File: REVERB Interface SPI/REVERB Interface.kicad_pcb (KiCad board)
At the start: 2 copper layers, 90.2 x 95.9 mm, 49 parts, among them J1 RPiZeroW, J2 Iridium, J3 APRS, J4 Antenna, J6 USB_B_Micro, J7 USB, J8 USBPOGO, M1 MountingHole_Pad, M2 MountingHole_Pad, M3 MountingHole_Pad, M4 MountingHole_Pad, M5 PiMount, M6 PiMount, M7 PiMount, M8 PiMount, U1 LSM9DS1BOB, U2 MAX3232, U3 CY7C65213-28PVXI

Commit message: spi edits
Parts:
- removed J6: USB_B_Micro, REVERB Interface:AdafruitMicroB
- removed J7: USB, Connector_PinSocket_2.54mm:PinSocket_1x02_P2.54mm_Vertical
- removed J8: USBPOGO, Connector_PinSocket_2.54mm:PinSocket_1x02_P2.54mm_Vertical
- added C9: 33pF, Capacitor_SMD:C_0805_2012Metric_Pad1.18x1.45mm_HandSolder, F.Cu at (230.2, 125.1)
- added R7: 1K, Resistor_SMD:R_0805_2012Metric_Pad1.20x1.40mm_HandSolder, F.Cu at (225.4, 128.1)
- added R8: 1K, Resistor_SMD:R_0805_2012Metric_Pad1.20x1.40mm_HandSolder, F.Cu at (230.1, 128.1)
- added Y1: 1.8432MHz, Crystal:Crystal_HC49-U_Vertical, F.Cu at (227.0, 120.3)
- C6: value 4.7uF -> 10uF
- C8: value 1uF -> 22pF
- JP3: value USBUARTRX -> SPIUARTRX
- JP4: value USBUARTTX -> SPIUARTTX
- U3: value CY7C65213-28PVXI -> SC16IS752IPW; footprint Package_SO:SSOP-28_5.3x10.2mm_P0.65mm -> Package_SO:TSSOP-28_4.4x9.7mm_P0.65mm
- moved C7 90.0 mm to (235.9, 134.6), turned to 0 degrees
- moved U3 83.9 mm to (240.3, 122.6)
- moved C6 82.1 mm to (231.1, 134.6), turned to 0 degrees
- moved C8 76.4 mm to (225.4, 125.1), turned to 0 degrees
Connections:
- C6 pad 1: /SW7 -> /SW10
- C7 pad 1: /SW7 -> /SW10
- D1 pad 1: /USBUARTTX -> /SPIUARTTX
- D2 pad 1: /USBUARTRX -> /SPIUARTRX
- H2 pad 16: /SW7 -> (no net)
- H2 pad 20: (no net) -> /SW10
- J1 pad 19: (no net) -> /SPIMOSI
- J1 pad 21: (no net) -> /SPIMISO
- J1 pad 23: (no net) -> /SPISCK
- J1 pad 24: (no net) -> /SPICE0
- JP3 pad 2: /USBUARTRX -> /SPIUARTRX
- JP4 pad 2: /USBUARTTX -> /SPIUARTTX
- R1 pad 1: /SW7 -> /SW10
- R2 pad 1: /SW7 -> /SW10
- R3 pad 1: /SW7 -> /SW10
- U3 pad 1: /USBUARTTX -> (no net)
- U3 pad 10: (no net) -> /SPICE0
- U3 pad 11: (no net) -> /SPIMOSI
- U3 pad 12: (no net) -> /SPIMISO
- U3 pad 13: (no net) -> /SPISCK
- U3 pad 14: (no net) -> GND
- U3 pad 15: /D+ -> Net-(R7-Pad2)
- U3 pad 16: /D- -> (no net)
- U3 pad 17: Net-(C8-Pad1) -> (no net)
- U3 pad 18: GND -> (no net)
- U3 pad 20: /SW7 -> (no net)
- U3 pad 21: GND -> (no net)
- U3 pad 22: (no net) -> GND
- U3 pad 3: (no net) -> /SPIUARTTX
- U3 pad 4: /SW7 -> /SPIUARTRX
- U3 pad 5: /USBUARTRX -> Net-(R8-Pad2)
- U3 pad 6: (no net) -> Net-(C8-Pad1)
- U3 pad 7: GND -> Net-(C9-Pad1)
- U3 pad 8: (no net) -> /SW10
- U3 pad 9: (no net) -> GND
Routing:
- net /SW7: track 122.6 -> 0.00 mm, vias 2 -> 0
- net /D+: track 79.8 -> 0.00 mm
- net /D-: track 73.7 -> 0.00 mm
- net /USBUARTRX: track 26.0 -> 0.00 mm, vias 2 -> 0
- net /USBUARTTX: track 23.8 -> 0.00 mm
- net GND: track 34.4 -> 19.7 mm, vias 18 -> 14
- net Net-(C8-Pad1): track 11.4 -> 0.00 mm, vias 2 -> 0
- net /SPIUARTTX: track 0.00 -> 10.2 mm
- net /SPIUARTRX: track 0.00 -> 9.14 mm
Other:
- board text removed: "D+"
- board text removed: "D-"
- board text removed: "Programming USB Header"

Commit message: SPI Branch routing
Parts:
- moved C7 87.5 mm to (148.6, 130.2), turned to 270 degrees
- moved C6 85.8 mm to (145.4, 130.2), turned to 270 degrees
- moved U3 84.9 mm to (155.6, 127.0)
- moved R8 82.4 mm to (147.8, 123.8), turned to 270 degrees
- moved C9 79.3 mm to (152.6, 141.6), turned to 180 degrees
- moved Y1 70.2 mm to (158.8, 136.5), turned to 180 degrees
- moved C8 67.5 mm to (160.0, 141.6)
- moved R7 63.6 mm to (161.9, 131.4), turned to 270 degrees
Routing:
- net /SW10: track 0.01 -> 124.6 mm, vias 0 -> 4
- net /SPICE0: track 0.00 -> 100.3 mm, vias 0 -> 3
- net /SPISCK: track 0.00 -> 94.6 mm, vias 0 -> 2
- net /SPIMISO: track 0.00 -> 89.1 mm, vias 0 -> 4
- net /SPIMOSI: track 0.00 -> 88.7 mm, vias 0 -> 4
- net Net-(C8-Pad1): track 0.00 -> 19.0 mm
- net Net-(C9-Pad1): track 0.00 -> 17.3 mm
- net /SPIUARTTX: track 10.2 -> 22.0 mm
- net /SPIUARTRX: track 9.14 -> 19.1 mm
- net GND: track 19.7 -> 25.9 mm, vias 14 -> 18
- net Net-(R8-Pad2): track 0.00 -> 5.11 mm
- net Net-(R7-Pad2): track 0.00 -> 3.95 mm

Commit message: update silkscreen
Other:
- board text added: "TJ REVERB INTERFACE BOARD Redesign Rev1, SPI Branch Designed by Alan Hsu, Class of '23"
- board text removed: "TJ REVERB INTERFACE BOARD Redesign Rev1 Designed by Alan Hsu, Class of '23"

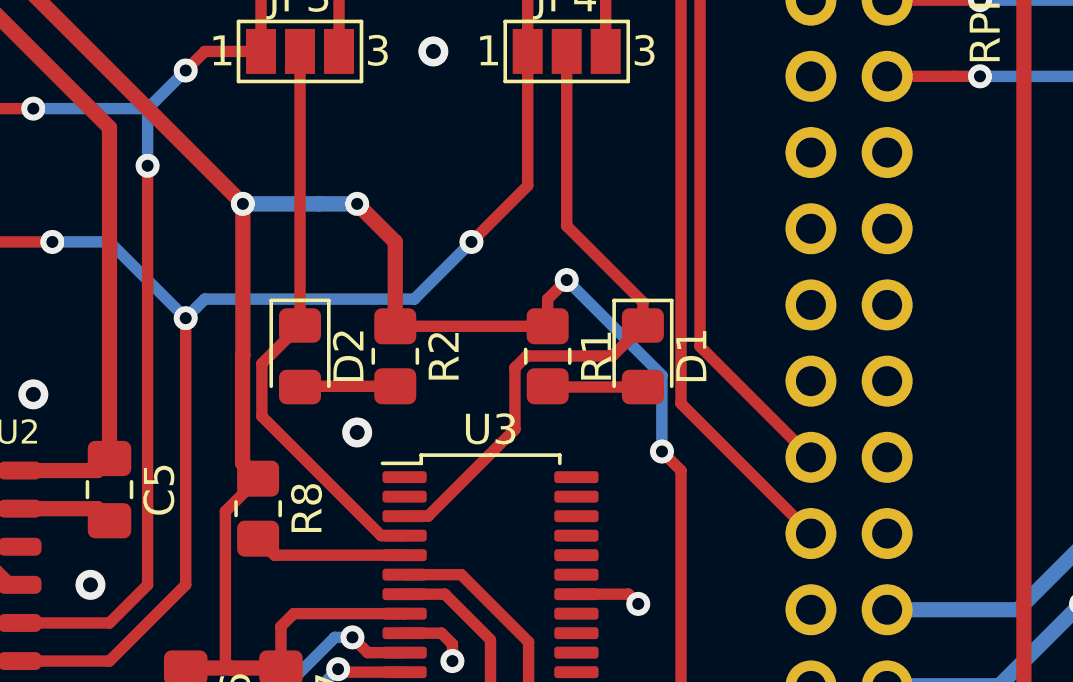
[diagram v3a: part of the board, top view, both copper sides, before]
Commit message: Add RTS and CTS connections to layout
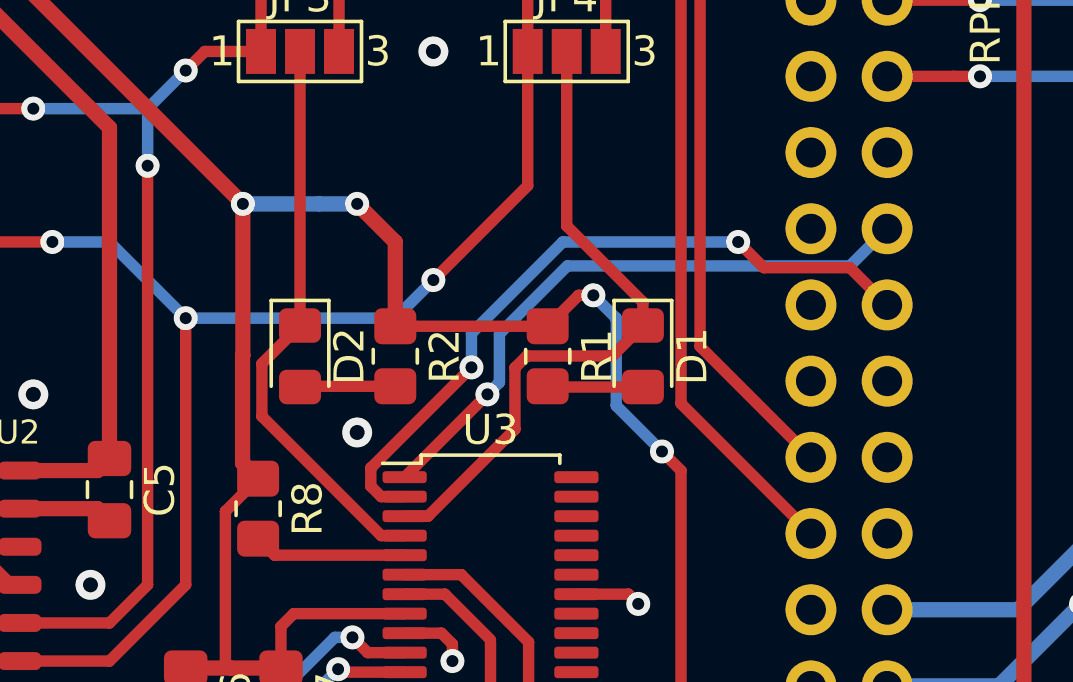
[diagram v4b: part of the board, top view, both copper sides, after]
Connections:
- J1 pad 13: (no net) -> /CTS
- J1 pad 15: (no net) -> /RTS
- U3 pad 1: (no net) -> /RTS
- U3 pad 2: (no net) -> /CTS
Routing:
- net /CTS: track 0.00 -> 23.7 mm, vias 0 -> 2
- net /RTS: track 0.00 -> 20.5 mm, vias 0 -> 1
- net /SW10: track 124.6 -> 123.9 mm

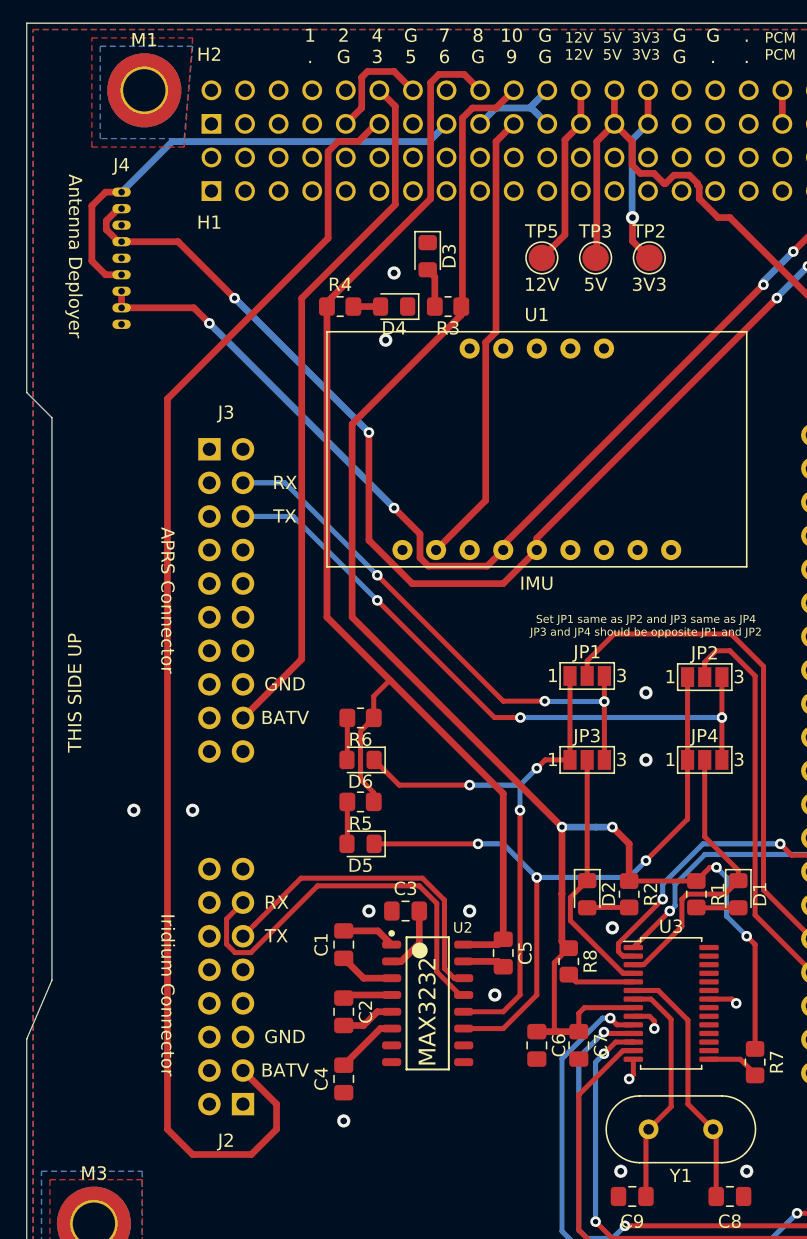
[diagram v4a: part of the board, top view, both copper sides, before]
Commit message: Add LEDs for all used PDMs
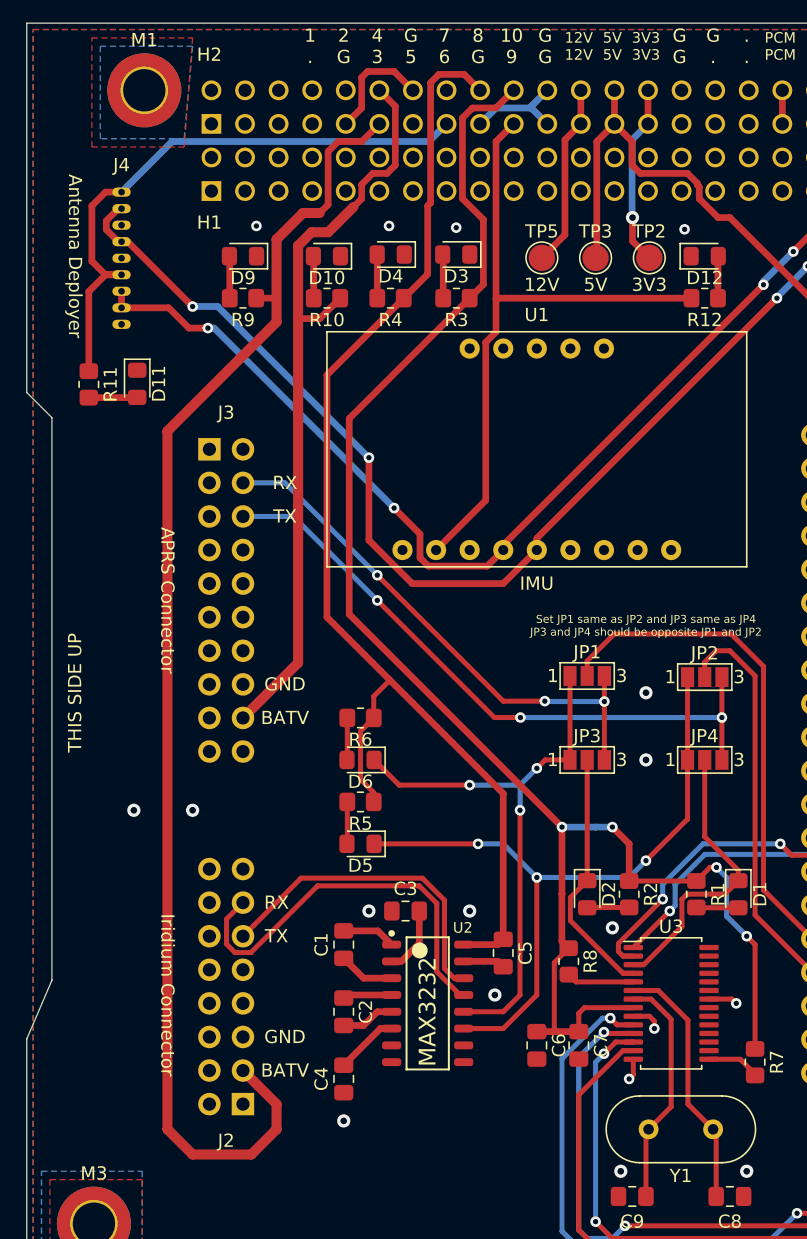
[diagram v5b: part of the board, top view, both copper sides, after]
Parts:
- added D10: RED, LED_SMD:LED_0805_2012Metric_Pad1.15x1.40mm_HandSolder, F.Cu at (129.5, 70.5)
- added D11: RED, LED_SMD:LED_0805_2012Metric_Pad1.15x1.40mm_HandSolder, F.Cu at (115.2, 80.1)
- added D12: RED, LED_SMD:LED_0805_2012Metric_Pad1.15x1.40mm_HandSolder, F.Cu at (158.1, 70.5)
- added D9: RED, LED_SMD:LED_0805_2012Metric_Pad1.15x1.40mm_HandSolder, F.Cu at (123.2, 70.5)
- added R10: 5K, Resistor_SMD:R_0805_2012Metric_Pad1.20x1.40mm_HandSolder, F.Cu at (129.5, 73.7)
- added R11: 1K, Resistor_SMD:R_0805_2012Metric_Pad1.20x1.40mm_HandSolder, F.Cu at (111.5, 80.2)
- added R12: 1K, Resistor_SMD:R_0805_2012Metric_Pad1.20x1.40mm_HandSolder, F.Cu at (158.1, 73.7)
- added R9: 5K, Resistor_SMD:R_0805_2012Metric_Pad1.20x1.40mm_HandSolder, F.Cu at (123.2, 73.7)
- moved D4 3.95 mm to (134.4, 70.4)
- moved R4 3.86 mm to (134.3, 73.7), turned to 180 degrees
- moved D3 2.16 mm to (139.3, 70.4), turned to 180 degrees
- moved R3 0.90 mm to (139.3, 73.7)
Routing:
- net /SW9: track 34.7 -> 49.5 mm
- net /SW6: track 36.2 -> 45.3 mm
- net /SW4: track 52.7 -> 57.9 mm
- net Net-(D11-Pad2): track 0.00 -> 3.67 mm
- net Net-(D10-Pad2): track 0.00 -> 3.19 mm
- net Net-(D9-Pad2): track 0.00 -> 3.19 mm
- net Net-(D12-Pad2): track 0.00 -> 3.19 mm
- net /SW3: track 99.1 -> 101.3 mm
- net /SW10: track 123.9 -> 125.5 mm
- net Net-(D4-Pad2): track 2.06 -> 3.31 mm
- net /EPSSDA: track 160.3 -> 159.2 mm
- net +5V: track 108.4 -> 107.9 mm
- net GND: vias 18 -> 20
